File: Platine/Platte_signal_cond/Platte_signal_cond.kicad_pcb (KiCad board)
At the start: 2 copper layers, 19 parts, among them J1 Conn_01x06, J2 Conn_01x07_MountingPin

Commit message: PCBs almost finished
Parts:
- moved J1 11.7 mm to (46.0, 74.2), turned to 90 degrees
- turned R6 to 90 degrees
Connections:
- U2 pad 4: +3.3VA -> +3.3VD
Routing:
- net +3.3VD: track 0.00 -> 48.3 mm, vias 0 -> 2
- net +3.3VA: track 0.00 -> 40.4 mm, vias 0 -> 1
- net /Out3: track 0.00 -> 22.8 mm
- net /data_in3: track 0.00 -> 19.5 mm
- net /data_in1: track 0.00 -> 15.8 mm, vias 0 -> 2
- net GNDA: track 0.00 -> 15.3 mm, vias 0 -> 1
- net /Out2: track 0.00 -> 12.0 mm
- net /Out1: track 0.00 -> 11.2 mm
- net GNDD: track 0.00 -> 8.53 mm, vias 0 -> 11
- net /Vin2-: track 0.00 -> 6.75 mm
- net /Vin3-: track 0.00 -> 6.31 mm
- net /Vin2+: track 0.00 -> 6.15 mm
- net /data_in2: track 0.00 -> 6.10 mm, vias 0 -> 2
- net /Vin1-: track 0.00 -> 5.46 mm
- net /Vin1+: track 0.00 -> 3.63 mm
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- added copper zone on B.Cu, net GNDA
- added copper zone on B.Cu, net GNDD
- added copper zone on F.Cu, net GNDD
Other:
- board outline added: 27.2 x 23.2 mm

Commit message: PCBs completely finished
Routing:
- net GNDD: track 8.53 -> 44.5 mm, vias 11 -> 19
- net +3.3VA: track 40.4 -> 42.4 mm
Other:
- board size 27.2 x 23.2 mm -> 28 x 23.2 mm
- board text added: "Out1 Out2 Out3 33VD VPlt GNDD"
- board text added: "VD GA GD"
- board text added: "d1 d2 d3 VA"

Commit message: PCBs ready
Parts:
- removed C1, C2, C3: 10n, Capacitor_SMD:C_0201_0603Metric_Pad0.64x0.40mm_HandSolder
- removed R1, R2, R3: 1k, Resistor_SMD:R_0201_0603Metric_Pad0.64x0.40mm_HandSolder
- C4, C5, C6: value 300p -> 1.85n; footprint Capacitor_SMD:C_0201_0603Metric_Pad0.64x0.40mm_HandSolder -> Capacitor_SMD:C_0603_1608Metric_Pad1.08x0.95mm_HandSolder
- R4, R5, R6: footprint Resistor_SMD:R_0201_0603Metric_Pad0.64x0.40mm_HandSolder -> Resistor_SMD:R_0603_1608Metric_Pad0.98x0.95mm_HandSolder
- R7, R8, R9: value 3.3k -> 270; footprint Resistor_SMD:R_0201_0603Metric_Pad0.64x0.40mm_HandSolder -> Resistor_SMD:R_0603_1608Metric_Pad0.98x0.95mm_HandSolder
- moved R4 0.90 mm to (52.2, 62.0)
- moved R9 0.40 mm to (65.0, 66.9)
- moved R5 0.15 mm to (52.8, 64.7), turned to 180 degrees
- moved R6 0.12 mm to (66.8, 66.8), turned to -90 degrees
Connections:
- J2 pad 5: /data_in3 -> /Vin3+
- J2 pad 6: /data_in2 -> /Vin1+
- J2 pad 7: /data_in1 -> /Vin2+
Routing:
- net /data_in3: track 19.5 -> 0.00 mm
- net GNDD: track 44.5 -> 26.5 mm, vias 19 -> 14
- net /data_in1: track 16.1 -> 0.00 mm, vias 2 -> 0
- net /Vin1+: track 3.63 -> 13.4 mm, vias 0 -> 2
- net /Vin3+: track 3.60 -> 10.2 mm, vias 0 -> 2
- net /data_in2: track 6.10 -> 0.00 mm, vias 2 -> 0
- net /Vin2+: track 6.15 -> 9.23 mm, vias 0 -> 2
- net GNDA: track 15.3 -> 16.1 mm
- net +3.3VD: track 48.3 -> 47.6 mm
- net /Vin1-: track 5.46 -> 6.06 mm
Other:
- board text added: "d2 d1 d3 VA"
- board text removed: "d1 d2 d3 VA"

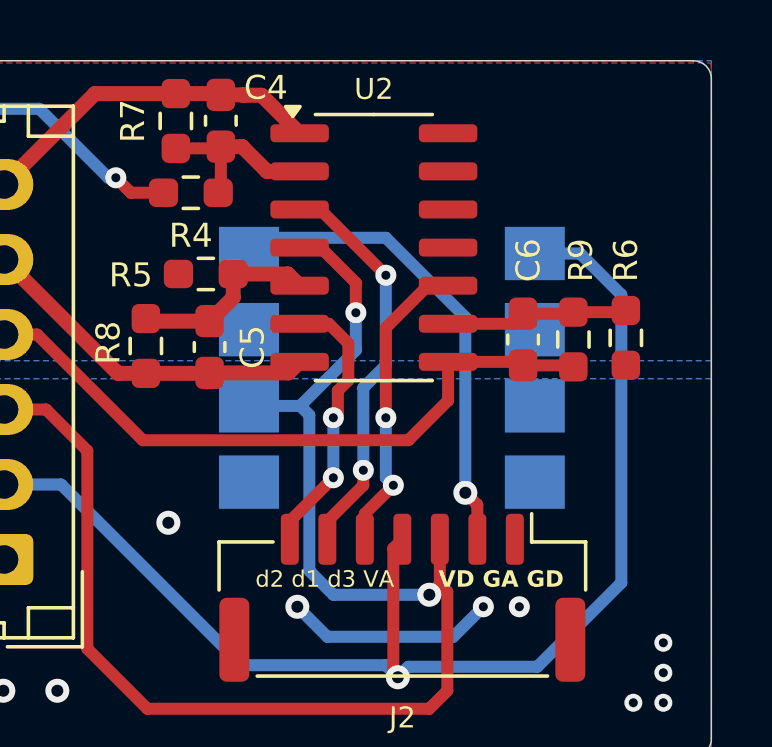
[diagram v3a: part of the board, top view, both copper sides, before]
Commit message: Modifying working frequency in LTSpice and adding extra resistor in pcb
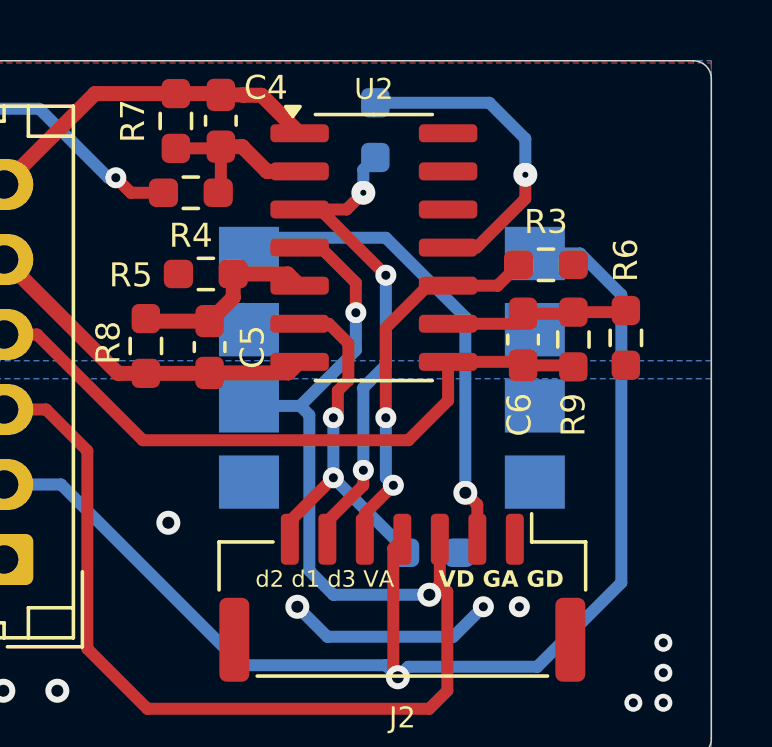
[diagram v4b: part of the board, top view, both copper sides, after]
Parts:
- added R1: 100k, Resistor_SMD:R_0603_1608Metric_Pad0.98x0.95mm_HandSolder, B.Cu at (58.4, 59.9)
- added R2: 100k, Resistor_SMD:R_0603_1608Metric_Pad0.98x0.95mm_HandSolder, B.Cu at (60.3, 74.0)
- added R3: 100k, Resistor_SMD:R_0603_1608Metric_Pad0.98x0.95mm_HandSolder, F.Cu at (64.1, 64.4)
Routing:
- net GNDD: track 26.5 -> 37.2 mm, vias 14 -> 15
- net /Vin1+: track 13.4 -> 17.1 mm, vias 2 -> 3
- net /Vin2+: track 9.23 -> 12.7 mm
- net /Vin3+: track 10.2 -> 12.8 mm

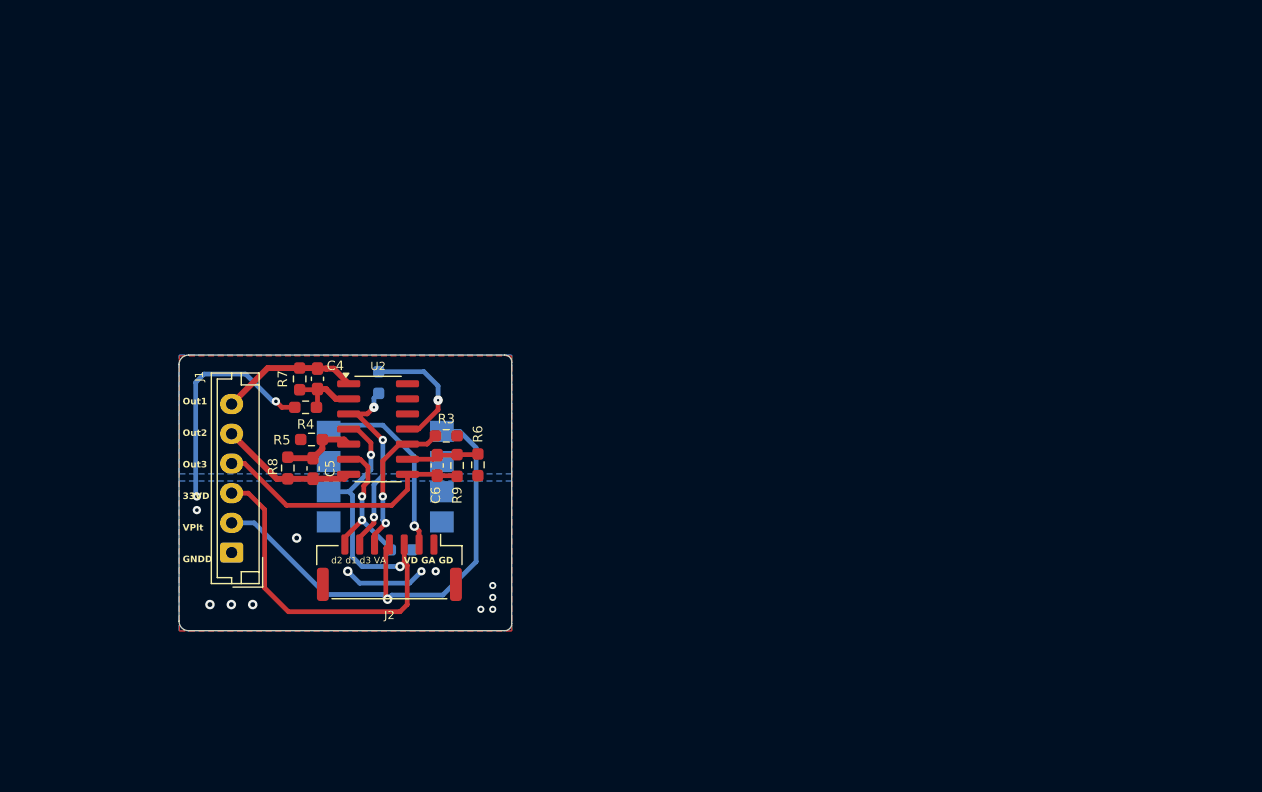
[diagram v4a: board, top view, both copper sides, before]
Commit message: Final circuits designed. Plate PCB ready, signal cond PCB still in process
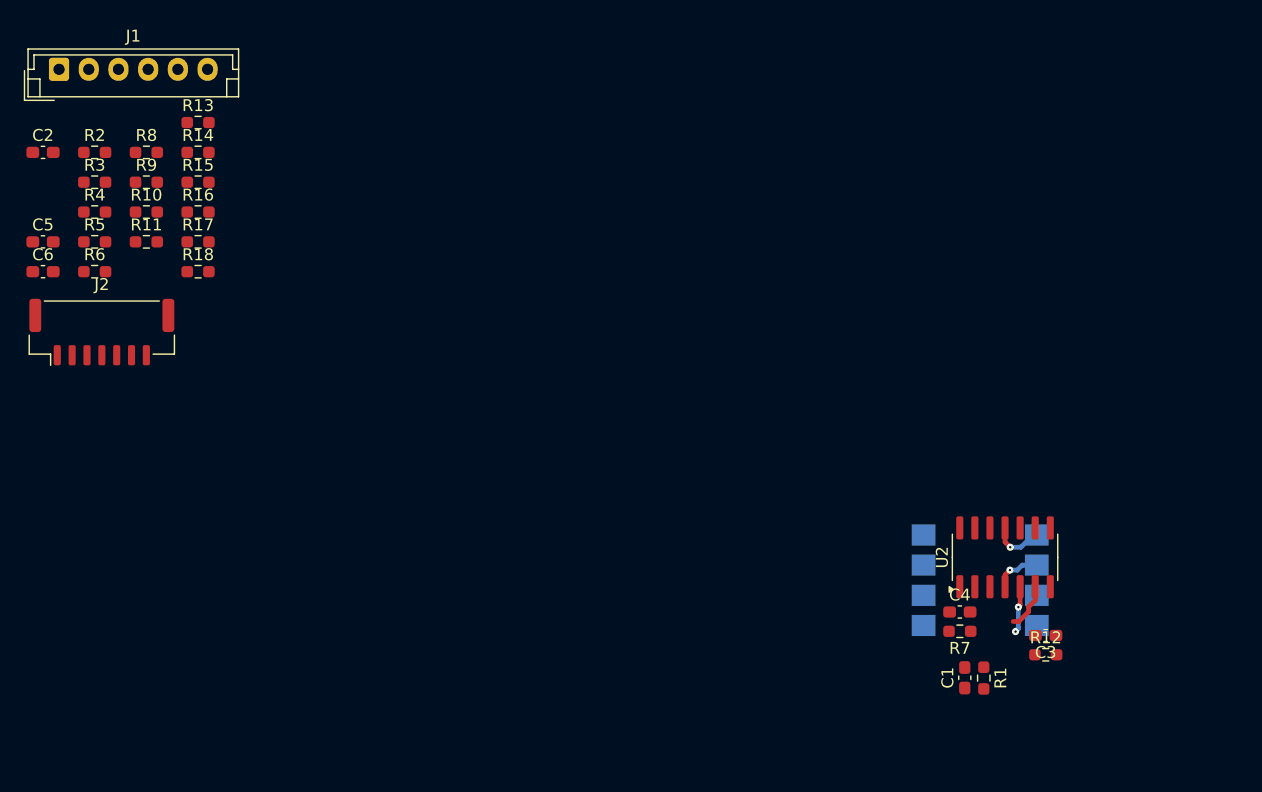
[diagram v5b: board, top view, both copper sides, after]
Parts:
- added C1: 100p, Capacitor_SMD:C_0603_1608Metric_Pad1.08x0.95mm_HandSolder, F.Cu at (107.7, 84.8)
- added C2: 100p, Capacitor_SMD:C_0603_1608Metric_Pad1.08x0.95mm_HandSolder, F.Cu at (30.1, 40.5)
- added C3: 100p, Capacitor_SMD:C_0603_1608Metric_Pad1.08x0.95mm_HandSolder, F.Cu at (114.5, 81.2)
- added R10: 100k, Resistor_SMD:R_0603_1608Metric_Pad0.98x0.95mm_HandSolder, F.Cu at (38.9, 45.6)
- added R11: 252k, Resistor_SMD:R_0603_1608Metric_Pad0.98x0.95mm_HandSolder, F.Cu at (38.9, 48.1)
- added R12: 252k, Resistor_SMD:R_0603_1608Metric_Pad0.98x0.95mm_HandSolder, F.Cu at (114.5, 82.8)
- added R13: 1k, Resistor_SMD:R_0603_1608Metric_Pad0.98x0.95mm_HandSolder, F.Cu at (43.2, 38.0)
- added R14: 1k, Resistor_SMD:R_0603_1608Metric_Pad0.98x0.95mm_HandSolder, F.Cu at (43.2, 40.5)
- added R15: 100k, Resistor_SMD:R_0603_1608Metric_Pad0.98x0.95mm_HandSolder, F.Cu at (43.2, 43.1)
- added R16: 100k, Resistor_SMD:R_0603_1608Metric_Pad0.98x0.95mm_HandSolder, F.Cu at (43.2, 45.6)
- added R17: 252k, Resistor_SMD:R_0603_1608Metric_Pad0.98x0.95mm_HandSolder, F.Cu at (43.2, 48.1)
- added R18: 252k, Resistor_SMD:R_0603_1608Metric_Pad0.98x0.95mm_HandSolder, F.Cu at (43.2, 50.6)
- C4, C5, C6: value 1.85n -> 100p
- R1: value 100k -> 252k; moved to F.Cu
- R2: moved to F.Cu
- R3: value 100k -> 1k
- R4: value 1k -> 100k
- R7: value 270 -> 252k
- R8: value 270 -> 1k
- R9: value 270 -> 100k
- moved R7 59.5 mm to (107.3, 80.8), turned to 180 degrees
- moved C4 57.5 mm to (107.3, 79.2), turned to 0 degrees
- moved R1 56.7 mm to (109.3, 84.8), turned to -90 degrees
- moved U2 53.9 mm to (111.1, 74.6), turned to 90 degrees
- moved U1 50.8 mm to (109.0, 76.5), turned to 180 degrees
- moved J1 43.2 mm to (31.5, 33.6), turned to 0 degrees
- moved R2 42.2 mm to (34.5, 40.5)
- moved C6 37.0 mm to (30.1, 50.6), turned to 0 degrees
- moved R3 36.5 mm to (34.5, 43.1)
- moved R6 36.1 mm to (34.5, 50.6), turned to 0 degrees
- moved R9 35.4 mm to (38.9, 43.1), turned to 0 degrees
- moved J2 31.3 mm to (35.1, 55.7), turned to 0 degrees
- moved C5 29.7 mm to (30.1, 48.1), turned to 0 degrees
- moved R8 29.1 mm to (38.9, 40.5), turned to 0 degrees
- moved R5 24.7 mm to (34.5, 48.1), turned to 0 degrees
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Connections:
- C4 pad 1: /Vin1- -> /Out1
- C4 pad 2: /Out1 -> /Vin1-
- C5 pad 1: /Vin2- -> GNDD
- C5 pad 2: /Out2 -> /Vin3+
- C6 pad 1: /Vin3- -> /Out3
- C6 pad 2: /Out3 -> /Vin3-
- J2 pad 5: /Vin3+ -> /data_in3
- J2 pad 6: /Vin1+ -> /data_in1
- J2 pad 7: /Vin2+ -> /data_in2
- R2 pad 1: /Vin2+ -> /Vin1+
- R2 pad 2: GNDD -> Net-(R2-Pad2)
- R3 pad 1: /Vin3+ -> +3.3VD
- R3 pad 2: GNDD -> Net-(R2-Pad2)
- R4 pad 2: GNDD -> /data_in1
- R5 pad 1: /Vin2- -> Net-(R2-Pad2)
- R6 pad 1: /Vin3- -> +3.3VD
- R6 pad 2: GNDD -> Net-(R6-Pad2)
- R8 pad 1: /Vin2- -> Net-(R6-Pad2)
- R8 pad 2: /Out2 -> GNDD
- R9 pad 1: /Vin3- -> /Vin2+
- R9 pad 2: /Out3 -> Net-(R6-Pad2)
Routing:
- net +3.3VD: track 47.6 -> 4.01 mm, vias 2 -> 1
- net +3.3VA: track 42.4 -> 0.00 mm, vias 1 -> 0
- net GNDD: track 37.2 -> 4.47 mm, vias 15 -> 1
- net /Out3: track 22.3 -> 0.00 mm
- net /Vin1+: track 17.1 -> 0.00 mm, vias 3 -> 0
- net GNDA: track 16.1 -> 0.00 mm, vias 1 -> 0
- net /Vin3+: track 12.8 -> 0.00 mm, vias 2 -> 0
- net /Out1: track 11.7 -> 0.00 mm
- net /Out2: track 11.6 -> 0.00 mm
- net /Vin2+: track 12.7 -> 3.97 mm, vias 2 -> 0
- net /Vin3-: track 6.11 -> 0.00 mm
- net /Vin1-: track 6.06 -> 0.00 mm
- net /Vin2-: track 6.43 -> 4.35 mm, vias 0 -> 2
- removed copper zone on B.Cu, net GNDA
- removed copper zone on B.Cu, net GNDD
- removed copper zone on F.Cu, net GNDD
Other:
- board outline removed
- board text removed: "Out1 Out2 Out3 33VD VPlt GNDD"
- board text removed: "VD GA GD"
- board text removed: "d2 d1 d3 VA"

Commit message: Made a few changes to PCBs and schematics
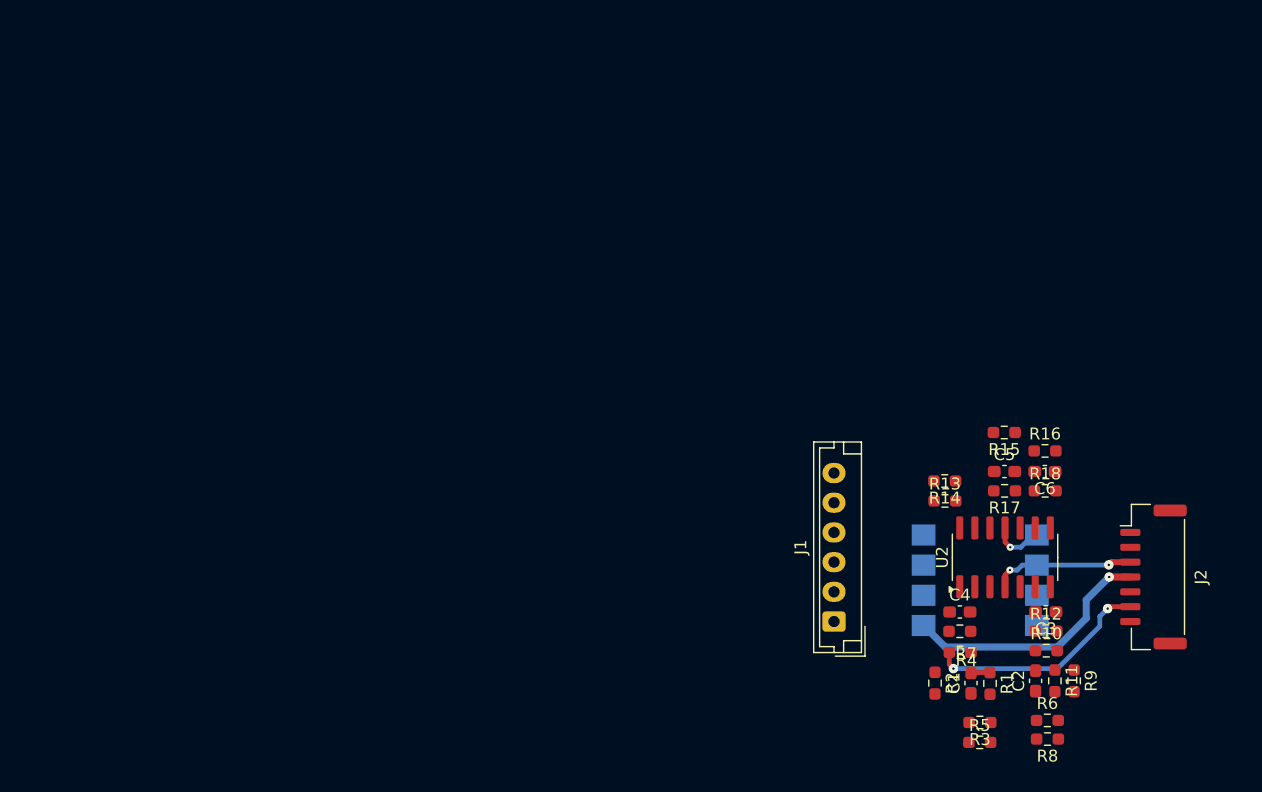
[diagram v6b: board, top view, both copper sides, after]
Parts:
- moved C2 94.6 mm to (113.7, 85.0), turned to 90 degrees
- moved J2 90.9 mm to (123.6, 76.3), turned to -90 degrees
- moved R8 90.5 mm to (114.7, 89.9), turned to 180 degrees
- moved R9 88.6 mm to (116.9, 85.0), turned to -90 degrees
- moved R6 88.6 mm to (114.7, 88.3)
- moved R3 87.3 mm to (109.0, 88.5), turned to 180 degrees
- moved C6 86.0 mm to (114.5, 67.4), turned to 180 degrees
- moved R5 85.6 mm to (109.0, 90.2)
- moved R11 84.9 mm to (115.3, 85.0), turned to -90 degrees
- moved R10 84.3 mm to (114.6, 82.5)
- moved R2 83.6 mm to (105.2, 85.2), turned to -90 degrees
- moved C5 83.2 mm to (111.1, 67.4)
- moved R4 81.7 mm to (107.3, 82.6), turned to 180 degrees
- moved J1 80.1 mm to (96.7, 80.0), turned to 90 degrees
- moved R16 74.1 mm to (114.5, 65.7)
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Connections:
- J1 pad 4: /Out3 -> /Out2
- J1 pad 5: /Out2 -> /Out1
- J1 pad 6: /Out1 -> /Out3
- U2 pad 5: /Vin2- -> /Vin2+
- U2 pad 6: /Vin2+ -> /Vin2-
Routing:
- net +3.3VA: track 0.00 -> 21.5 mm, vias 0 -> 1
- net /data_in1: track 0.00 -> 19.0 mm, vias 0 -> 2
- net +3.3VD: track 4.01 -> 12.0 mm, vias 1 -> 2
- net /Vin2-: track 4.35 -> 0.00 mm, vias 2 -> 0
- net /Vin2+: track 3.97 -> 0.00 mm
- net /Vin1+: track 0.00 -> 1.61 mm

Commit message: Both the PCBs finished
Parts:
- added M1: MountingHole_2.1mm, MountingHole:MountingHole_2.1mm, F.Cu at (93.6, 62.2)
- added M2: MountingHole_2.1mm, MountingHole:MountingHole_2.1mm, F.Cu at (124.5, 62.3)
- added M3: MountingHole_2.1mm, MountingHole:MountingHole_2.1mm, F.Cu at (93.7, 89.8)
- added M4: MountingHole_2.1mm, MountingHole:MountingHole_2.1mm, F.Cu at (124.5, 89.8)
- moved R2 0.97 mm to (105.5, 86.2)
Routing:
- net /Out2: track 0.00 -> 50.2 mm, vias 0 -> 2
- net +3.3VD: track 12.0 -> 49.2 mm, vias 2 -> 4
- net /Out3: track 0.00 -> 27.2 mm, vias 0 -> 1
- net GNDA: track 0.00 -> 24.3 mm, vias 0 -> 1
- net /Out1: track 0.00 -> 17.6 mm
- net /data_in3: track 0.00 -> 17.0 mm
- net /Vin2+: track 0.00 -> 11.1 mm
- net /Vin1+: track 1.61 -> 12.0 mm
- net +3.3VA: track 21.5 -> 30.4 mm, vias 1 -> 2
- net /Vin3+: track 0.00 -> 8.23 mm
- net Net-(R13-Pad2): track 0.00 -> 7.90 mm
- net /data_in2: track 0.00 -> 7.18 mm
- net /Vin3-: track 0.00 -> 6.54 mm
- net GNDD: track 4.47 -> 10.3 mm, vias 1 -> 11
- net /Vin1-: track 0.00 -> 5.72 mm
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- added copper zone on B.Cu, net GNDA
- added copper zone on B.Cu, net GNDD
- added copper zone on F.Cu, net GNDD
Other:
- board outline added: 35.8 x 32.5 mm
- board text added: "O D3 O D1 O D2 I VD I VP I GD"
- board text added: "O GD O GA O VD O VA I D3 I D1 I D2"

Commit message: Small correction. Everything finished
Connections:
- J1 pad 2: +3.3VA -> GNDA
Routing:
- net GNDA: track 24.3 -> 39.1 mm
- net +3.3VA: track 30.4 -> 21.6 mm, vias 2 -> 1
- net +3.3VD: track 49.2 -> 49.8 mm
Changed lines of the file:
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@@
 			(layers "*.Cu" "*.Mask")
 			(remove_unused_layers no)
-			(net 12 "+3.3VA")
+			(net 13 "GNDA")
 			(pinfunction "Pin_2")
 			(pintype "passive")
@@
 	)
 	(segment
-		(start 100.12 73.41)
-		(end 98.5 75.03)
-		(width 0.5)
-		(layer "F.Cu")
-		(net 11)
-	)
-	(segment
 		(start 121.66 75.03)
 		(end 120.08 75.03)
@@
 	)
 	(segment
+		(start 99.3 73.41)
+		(end 97.68 75.03)
+		(width 0.5)
+		(layer "F.Cu")
+		(net 11)
+	)
+	(segment
 		(start 111.115 77.1)
 		(end 111.115 83.305)
@@
 	)
 	(segment
-		(start 98.5 75.03)
-		(end 96.72 75.03)
-		(width 0.5)
+		(start 101.7 70)
+		(end 101.82 69.88)
+		(width 0.4)
 		(layer "F.Cu")
 		(net 11)
@@
 	)
 	(segment
+		(start 97.68 75.03)
+		(end 96.72 75.03)
+		(width 0.5)
+		(layer "F.Cu")
+		(net 11)
+	)
+	(segment
 		(start 110.375 88.525)
 		(end 109.9125 88.525)
@@
 	)
 	(segment
+		(start 101.82 69.88)
+		(end 103.3 69.88)
+		(width 0.4)
+		(layer "F.Cu")
+		(net 11)
+	)
+	(segment
 		(start 105.145 69.88)
 		(end 105.145 72.695)
@@
 	)
 	(segment
-		(start 105.145 69.88)
-		(end 102.84 69.88)
-		(width 0.5)
-		(layer "F.Cu")
-		(net 11)
-	)
-	(segment
 		(start 111.69 88.35)
 		(end 111.12 87.78)
@@
 	)
 	(segment
-		(start 102.84 69.88)
-		(end 102.7 70.02)
+		(start 107.09 74.64)
+		(end 110.465 74.64)
 		(width 0.4)
 		(layer "F.Cu")
@@
 	)
 	(segment
-		(start 107.09 74.64)
-		(end 110.465 74.64)
-		(width 0.4)
+		(start 105.145 69.88)
+		(end 103.3 69.88)
+		(width 0.5)
 		(layer "F.Cu")
 		(net 11)
@@
 	)
 	(via
-		(at 102.7 70.02)
+		(at 101.7 70)
 		(size 0.8)
 		(drill 0.2)
@@
 	)
 	(via
-		(at 100.12 73.41)
+		(at 99.3 73.41)
 		(size 0.8)
 		(drill 0.2)
@@
 	)
 	(segment
-		(start 100.12 72.6)
-		(end 100.12 73.41)
-		(width 0.5)
-		(layer "B.Cu")
-		(net 11)
-	)
-	(segment
 		(start 119.09 74.5)
 		(end 119.85 75.26)
@@
 	)
 	(segment
+		(start 100.8 70)
+		(end 99.3 71.5)
+		(width 0.5)
+		(layer "B.Cu")
+		(net 11)
+	)
+	(segment
 		(start 113.79 75.28)
 		(end 114.57 74.5)
@@
 	)
 	(segment
-		(start 102.7 70.02)
-		(end 100.12 72.6)
+		(start 99.3 71.5)
+		(end 99.3 73.41)
+		(width 0.5)
+		(layer "B.Cu")
+		(net 11)
+	)
+	(segment
+		(start 101.7 70)
+		(end 100.8 70)
 		(width 0.5)
 		(layer "B.Cu")
@@
 		(net 12)
 	)
-	(segment
-		(start 96.99 77.8)
-		(end 96.72 77.53)
-		(width 0.6)
-		(layer "F.Cu")
-		(net 12)
-	)
-	(segment
-		(start 99.4 77.8)
-		(end 96.99 77.8)
-		(width 0.6)
-		(layer "F.Cu")
-		(net 12)
-	)
-	(segment
-		(start 100.1 78.5)
-		(end 99.4 77.8)
-		(width 0.6)
-		(layer "F.Cu")
-		(net 12)
-	)
-	(via
-		(at 100.1 78.5)
-		(size 0.8)
-		(drill 0.2)
-		(layers "F.Cu" "B.Cu")
-		(net 12)
-	)
 	(via
 		(at 119.88 76.28)
@@
 	)
 	(segment
-		(start 100.6 78.5)
-		(end 102.46 80.36)
-		(width 0.6)
-		(layer "B.Cu")
-		(net 12)
-	)
-	(segment
 		(start 117.2 80.5)
 		(end 115.525 82.175)
@@
 	)
 	(segment
-		(start 100.1 78.5)
-		(end 100.6 78.5)
-		(width 0.6)
-		(layer "B.Cu")
-		(net 12)
-	)
-	(segment
 		(start 117.2 78.7)
 		(end 117.2 80.5)
@@
 	)
 	(segment
-		(start 102.46 80.36)
-		(end 104.26 80.36)
-		(width 0.6)
-		(layer "B.Cu")
-		(net 12)
-	)
-	(segment
 		(start 119.75 72.95)
 		(end 120.58 73.78)
@@
 	)
 	(segment
+		(start 96.99 77.8)
+		(end 96.72 77.53)
+		(width 0.6)
+		(layer "F.Cu")
+		(net 13)
+	)
+	(segment
 		(start 120.58 73.78)
 		(end 121.66 73.78)
@@
 	)
 	(segment
+		(start 103 70.7)
+		(end 102.1 71.6)
+		(width 0.5)
+		(layer "B.Cu")
+		(net 13)
+	)
+	(segment
 		(start 117.5 70.7)
 		(end 111.8 70.7)
@@
 	)
 	(segment
-		(start 109.8 72.7)
-		(end 109.8 78.1)
+		(start 99.77 77.53)
+		(end 96.72 77.53)
 		(width 0.5)
 		(layer "B.Cu")
@@
 	)
 	(segment
-		(start 109.8 78.1)
-		(end 112.06 80.36)
+		(start 102.1 75.2)
+		(end 99.77 77.53)
 		(width 0.5)
 		(layer "B.Cu")
@@
 	(segment
 		(start 111.8 70.7)
-		(end 109.8 72.7)
+		(end 103 70.7)
+		(width 0.5)
+		(layer "B.Cu")
+		(net 13)
+	)
+	(segment
+		(start 102.1 71.6)
+		(end 102.1 75.2)
+		(width 0.5)
+		(layer "B.Cu")
+		(net 13)
+	)
+	(segment
+		(start 109.6 70.7)
+		(end 107.7 72.6)
 		(width 0.5)
 		(layer "B.Cu")
@@
 	)
 	(segment
-		(start 112.06 80.36)
-		(end 113.79 80.36)
+		(start 107.7 72.6)
+		(end 107.7 77.5)
 		(width 0.5)
 		(layer "B.Cu")
